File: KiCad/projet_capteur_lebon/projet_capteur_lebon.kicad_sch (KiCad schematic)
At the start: 19 parts, among them J1 Power, J2 Digital/PWM, J3 Analog, J4 Digital/PWM

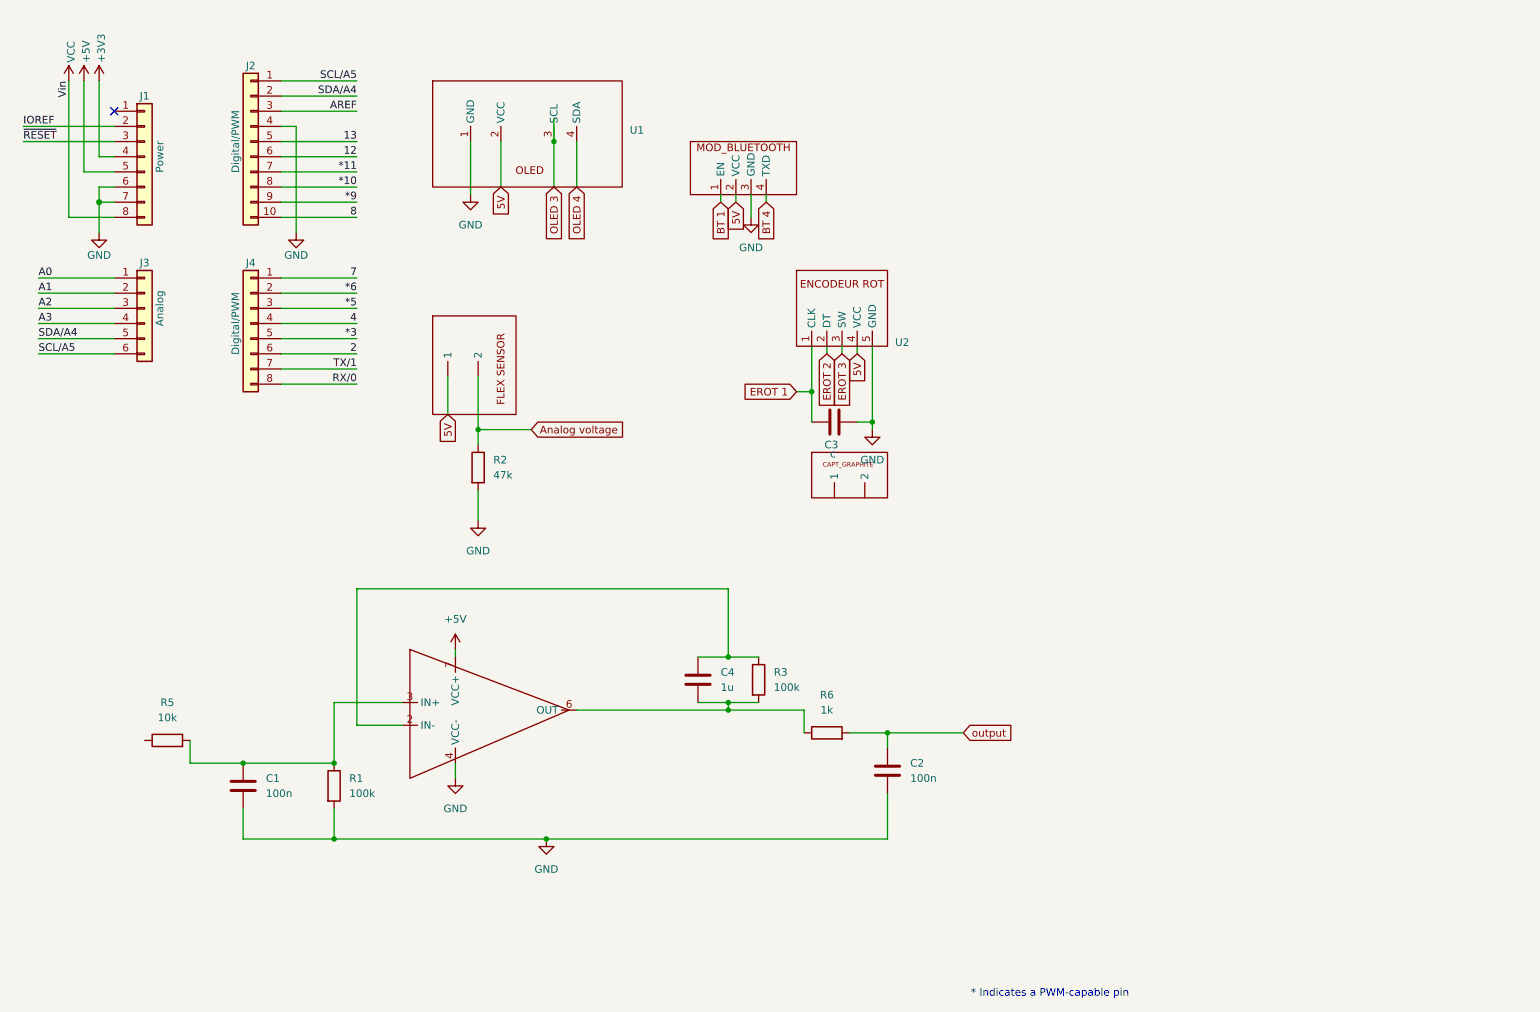
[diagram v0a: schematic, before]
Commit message: etiquettes + digital pot
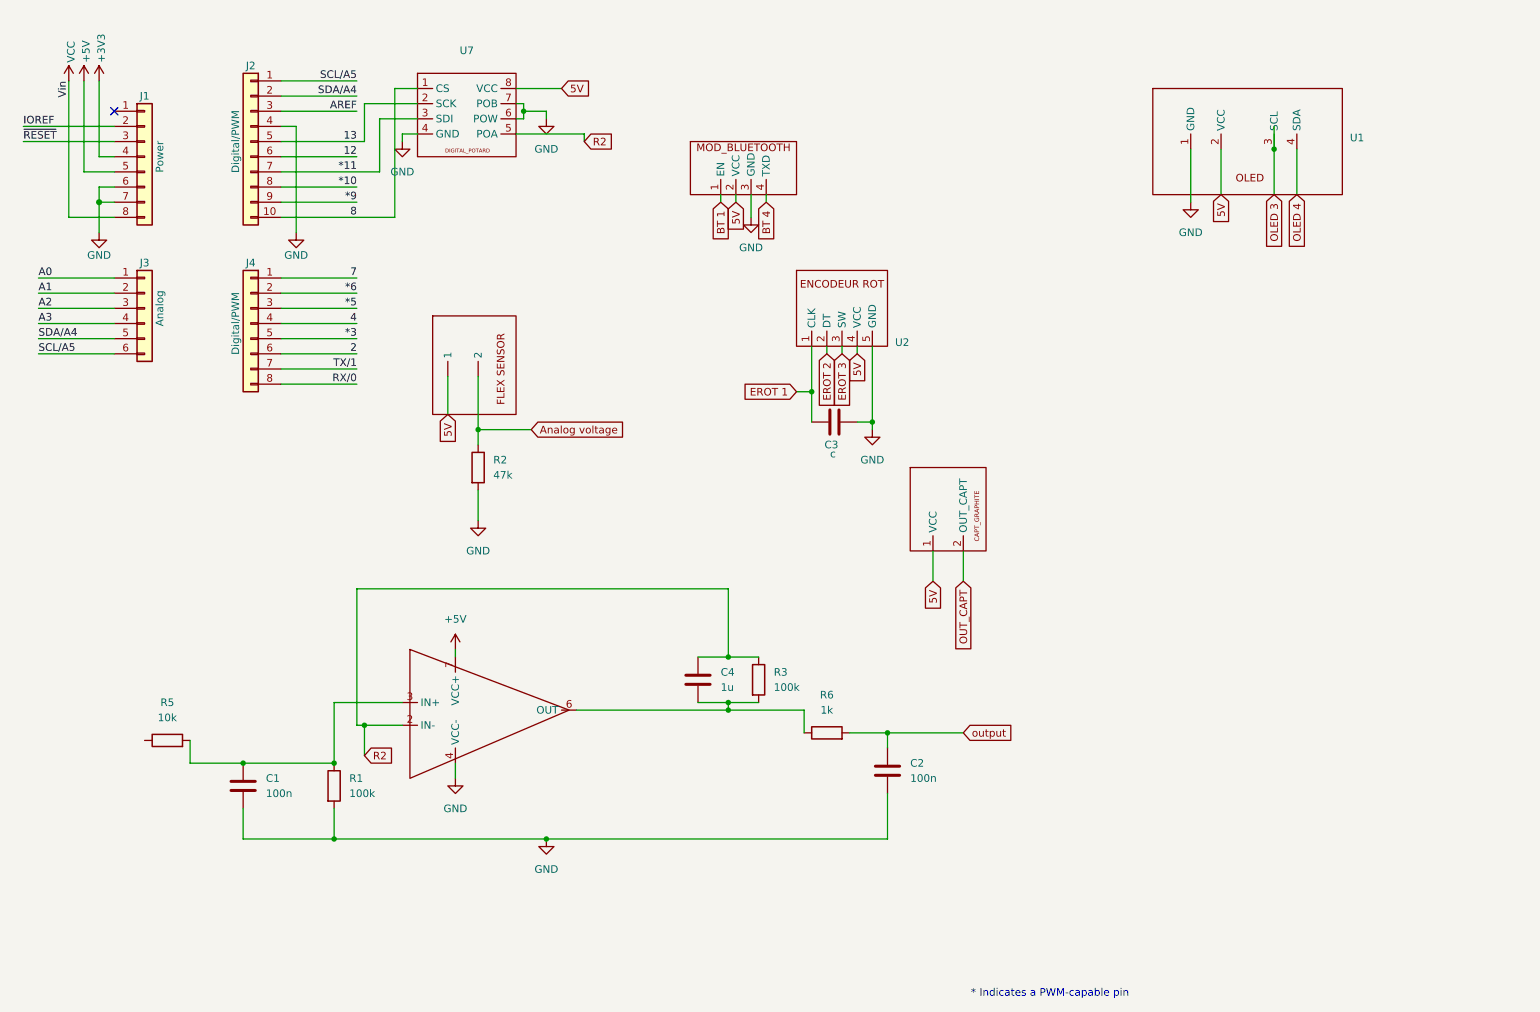
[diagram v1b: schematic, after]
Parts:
- removed U6: ~, librairie_empreintes:CAPTEUR_GRAPHITE, symbol librairie symboles:CAPTEUR_GRAPHITE
- added U7: ~, librairie_empreintes:DIP-8_296, symbol librairie symboles:DIGIT_POTARD
- added U8: ~, librairie_empreintes:CAPTEUR_GRAPHITE, symbol librairie symboles:CAPTEUR_GRAPHITE
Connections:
- net *11: now also U7.3 (SDI)
- net 13: now also U7.2 (SCK)
- net 5V: now also U7.8 (VCC), U8.1 (VCC)
- net 8: now also U7.1 (CS)
- net GND: now also U7.4 (GND), U7.6 (POW), U7.7 (POB)
- net R2: now reaches C4.1, R3.1, U4.2 (IN-)
- net R2: now also U7.5 (POA)
- new net OUT_CAPT: U8.2 (OUT_CAPT)
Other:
- moved on the sheet: U1

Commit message: fin schématique liaisons etc reste debug U5
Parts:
- removed U3: ~, librairie_empreintes:SIP-2, symbol librairie symboles:MOD_BLUETOOTH
- added U6: ~, librairie_empreintes:SIP-3, symbol librairie symboles:SERVOMOTOR
- added U9: ~, librairie_empreintes:BLUETOOTH, symbol librairie symboles:MOD_BLUETOOTH
- U5: footprint librairie_empreintes:BLUETOOTH -> librairie_empreintes:SIP-2
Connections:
- net AREF is gone; now on net 13: J2.3 (Pin_3)
- net Analog voltage is gone; now on net OUT_FLEX: R2.1, U5. (2)
- net EROT 1 is gone; now on net CLK: C3.1, U2.1 (CLK)
- net EROT 2 is gone; now on net DT: U2.2 (DT)
- net EROT 3 is gone; now on net SW: U2.3 (SW)
- net SCL/A5 is gone; now on net SCL: J2.1 (Pin_1), J3.6 (Pin_6)
- net SDA/A4 is gone; now on net SDA: J2.2 (Pin_2), J3.5 (Pin_5)
- net output is gone; now on net CAPT_AMPL: C2.1, R6.2
- net *10: now also U7.1 (CS)
- net *9: now also U6.1 (Data)
- net +5V: no longer J1.5 (Pin_5)
- net 5V: now also J1.5 (Pin_5), U6.2 (VCC), U9.2 (VCC)
- net GND: now also U6.3 (GND), U9.3 (GND)
- net OUT_CAPT: now also R5.1
- net *6 renamed SW
- net 2 renamed CLK
- net 4 renamed DT
- net 7 renamed RX
- net RX: now also U9.5 (RX)
- net 8 renamed TXD
- net TXD: now also U9.4 (TXD); no longer U7.1 (CS)
- net A0 renamed CAPT_AMPL
- net A1 renamed OUT_FLEX
- net OLED 3 renamed SCL
- net OLED 4 renamed SDA
- no-connect marks 1 -> 12
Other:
- moved on the sheet: C1, C2, C3, C4, J1, J2, J3, J4, R1, R2, R3, R5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

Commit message: modeles 3d et routage
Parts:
- renumbered R2 to R4
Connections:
- net +5V is gone; now on net 5V: U4.7 (VCC+)
- net 13: no longer J2.3 (Pin_3)
- net 5V: now also U5.1 (Vcc); no longer U5. (2)
- net OUT_FLEX: now also U5.2 (Out); no longer U5. (2)
- new net AREF: J2.3 (Pin_3)
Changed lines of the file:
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@@
 	)
 	(junction
-		(at 83.82 29.21)
-		(diameter 0)
-		(color 0 0 0 0)
-	)
-	(junction
 		(at 92.71 101.6)
 		(diameter 0)
@@
 	)
 	(junction
-		(at 71.12 41.91)
-		(diameter 0)
-		(color 0 0 0 0)
-	)
-	(junction
 		(at 153.67 90.17)
 		(diameter 0)
@@
 	)
 	(junction
-		(at 71.12 44.45)
-		(diameter 0)
-		(color 0 0 0 0)
-	)
-	(junction
 		(at 110.49 29.21)
 		(diameter 0)
@@
 	(wire
 		(pts
-			(xy 69.85 41.91) (xy 71.12 41.91)
-		)
-		(stroke
-			(width 0)
-			(type solid)
-		)
-	)
-	(wire
-		(pts
 			(xy 114.3 30.48) (xy 114.3 29.21)
 		)
@@
 	(wire
 		(pts
-			(xy 88.9 25.4) (xy 88.9 41.91)
+			(xy 87.63 25.4) (xy 87.63 41.91)
 		)
 		(stroke
@@
 	(wire
 		(pts
-			(xy 40.64 36.83) (xy 43.18 36.83)
+			(xy 85.09 34.29) (xy 85.09 27.94)
 		)
 		(stroke
@@
 	(wire
 		(pts
-			(xy 38.1 39.37) (xy 43.18 39.37)
+			(xy 40.64 36.83) (xy 43.18 36.83)
 		)
 		(stroke
@@
 	(wire
 		(pts
-			(xy 38.1 24.13) (xy 38.1 39.37)
+			(xy 38.1 39.37) (xy 43.18 39.37)
 		)
 		(stroke
@@
 	(wire
 		(pts
-			(xy 148.59 97.79) (xy 153.67 97.79)
+			(xy 38.1 24.13) (xy 38.1 39.37)
 		)
 		(stroke
 			(width 0)
-			(type default)
+			(type solid)
 		)
 	)
 	(wire
 		(pts
-			(xy 83.82 27.94) (xy 83.82 29.21)
+			(xy 148.59 97.79) (xy 153.67 97.79)
 		)
 		(stroke
@@
 	(wire
 		(pts
-			(xy 71.12 34.29) (xy 83.82 34.29)
+			(xy 71.12 34.29) (xy 85.09 34.29)
 		)
 		(stroke
@@
 	(wire
 		(pts
-			(xy 92.71 25.4) (xy 88.9 25.4)
+			(xy 92.71 25.4) (xy 87.63 25.4)
 		)
 		(stroke
@@
 	(wire
 		(pts
-			(xy 71.12 41.91) (xy 88.9 41.91)
+			(xy 71.12 44.45) (xy 92.71 44.45)
 		)
 		(stroke
 			(width 0)
-			(type solid)
+			(type default)
 		)
 	)
@@
 	(wire
 		(pts
-			(xy 92.71 27.94) (xy 83.82 27.94)
-		)
-		(stroke
-			(width 0)
-			(type default)
-		)
-	)
-	(wire
-		(pts
 			(xy 209.55 38.1) (xy 209.55 48.26)
 		)
@@
 	(wire
 		(pts
-			(xy 30.48 64.77) (xy 43.18 64.77)
-		)
-		(stroke
-			(width 0)
-			(type solid)
-		)
-	)
-	(wire
-		(pts
-			(xy 214.63 38.1) (xy 214.63 45.72)
+			(xy 71.12 41.91) (xy 87.63 41.91)
 		)
 		(stroke
@@
 	(wire
 		(pts
-			(xy 71.12 44.45) (xy 92.71 44.45)
+			(xy 30.48 64.77) (xy 43.18 64.77)
 		)
 		(stroke
 			(width 0)
-			(type default)
+			(type solid)
 		)
 	)
 	(wire
 		(pts
-			(xy 83.82 29.21) (xy 83.82 34.29)
+			(xy 214.63 38.1) (xy 214.63 45.72)
 		)
 		(stroke
@@
 	(wire
 		(pts
-			(xy 71.12 67.31) (xy 83.82 67.31)
+			(xy 85.09 27.94) (xy 92.71 27.94)
 		)
 		(stroke
@@
 	(wire
 		(pts
-			(xy 153.67 90.17) (xy 158.75 90.17)
+			(xy 71.12 67.31) (xy 83.82 67.31)
 		)
 		(stroke
 			(width 0)
-			(type default)
+			(type solid)
 		)
 	)
 	(wire
 		(pts
-			(xy 72.39 107.95) (xy 87.63 107.95)
+			(xy 153.67 90.17) (xy 158.75 90.17)
 		)
 		(stroke
@@
 	(wire
 		(pts
-			(xy 69.85 44.45) (xy 71.12 44.45)
+			(xy 72.39 107.95) (xy 87.63 107.95)
 		)
 		(stroke
@@
 	)
 	(label "*10"
-		(at 82.55 41.91 180)
+		(at 81.28 41.91 180)
 		(effects
 			(font
@@
 		)
 	)
+	(global_label "5V"
+		(shape input)
+		(at 107.95 88.9 90)
+		(fields_autoplaced yes)
+		(effects
+			(font
+				(size 1.27 1.27)
+			)
+			(justify left)
+		)
+		(property "Intersheetrefs" "${INTERSHEET_REFS}"
+			(at 107.95 83.5216 90)
+			(effects
+				(font
+					(size 1.27 1.27)
+				)
+				(justify left)
+				(hide yes)
+			)
+		)
+	)
 	(global_label "OUT_FLEX"
 		(shape input)
@@
 			)
 		)
-		(pin ""
+		(pin "2"
 		)
-		(pin ""
+		(pin "1"
 		)
 		(instances
@@
 		(dnp no)
 		(fields_autoplaced yes)
-		(property "Reference" "R2"
+		(property "Reference" "R4"
 			(at 223.52 81.2799 0)
 			(effects
@@
 			(project "projet_capteur_lebon"
 				(path "/e63e39d7-6ac0-4ffd-8aa3-1841a4541b55"
-					(reference "R2")
+					(reference "R4")
 					(unit 1)
 				)
@@
 					(unit 1)
 				)
-			)
-		)
-	)
-	(symbol
-		(lib_id "power:+5V")
-		(at 107.95 88.9 0)
-		(unit 1)
-		(exclude_from_sim no)
-		(in_bom yes)
-		(on_board yes)
-		(dnp no)
-		(fields_autoplaced yes)
-		(property "Reference" "#PWR07"
-			(at 107.95 92.71 0)
-			(effects
-				(font
-					(size 1.27 1.27)
-				)
-				(hide yes)
-			)
-		)
-		(property "Value" "+5V"
-			(at 107.95 83.82 0)
-			(effects
-				(font
-					(size 1.27 1.27)
-				)
-			)
-		)
-		(property "Footprint" ""
-			(at 107.95 88.9 0)
-			(effects
-				(font
-					(size 1.27 1.27)
-				)
-				(hide yes)
-			)
-		)
-		(property "Datasheet" ""
-			(at 107.95 88.9 0)
-			(effects
-				(font
-					(size 1.27 1.27)
-				)
-				(hide yes)
-			)
-		)
-		(property "Description" "Power symbol creates a global label with name \"+5V\""
-			(at 107.95 88.9 0)
-			(effects
-				(font
-					(size 1.27 1.27)
-				)
-				(hide yes)
-			)
-		)
-		(pin "1"
-		)
-		(instances
-			(project ""
-				(path "/e63e39d7-6ac0-4ffd-8aa3-1841a4541b55"
-					(reference "#PWR07")
-					(unit 1)
-				)

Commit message: finitions pcb et gerber
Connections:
- net GND: now also U7.5 (POA); no longer U7.7 (POB)
- net R2: now also U7.7 (POB); no longer U7.5 (POA)
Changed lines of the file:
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@@
 	)
 	(junction
-		(at 153.67 97.79)
+		(at 110.49 31.75)
 		(diameter 0)
 		(color 0 0 0 0)
 	)
 	(junction
-		(at 153.67 90.17)
+		(at 153.67 97.79)
 		(diameter 0)
 		(color 0 0 0 0)
 	)
 	(junction
-		(at 72.39 107.95)
+		(at 153.67 90.17)
 		(diameter 0)
 		(color 0 0 0 0)
 	)
 	(junction
-		(at 184.15 49.53)
+		(at 72.39 107.95)
 		(diameter 0)
 		(color 0 0 0 0)
 	)
 	(junction
-		(at 110.49 29.21)
+		(at 184.15 49.53)
 		(diameter 0)
 		(color 0 0 0 0)
@@
 	(wire
 		(pts
-			(xy 109.22 27.94) (xy 110.49 27.94)
+			(xy 109.22 27.94) (xy 119.38 27.94)
 		)
 		(stroke
@@
 	(wire
 		(pts
-			(xy 114.3 30.48) (xy 114.3 29.21)
-		)
-		(stroke
-			(width 0)
-			(type default)
-		)
-	)
-	(wire
-		(pts
 			(xy 71.12 24.13) (xy 83.82 24.13)
 		)
@@
 	(wire
 		(pts
+			(xy 114.3 31.75) (xy 114.3 35.56)
+		)
+		(stroke
+			(width 0)
+			(type default)
+		)
+	)
+	(wire
+		(pts
 			(xy 87.63 120.65) (xy 123.19 120.65)
 		)
@@
 	(wire
 		(pts
+			(xy 119.38 27.94) (xy 119.38 33.02)
+		)
+		(stroke
+			(width 0)
+			(type default)
+		)
+	)
+	(wire
+		(pts
+			(xy 110.49 33.02) (xy 109.22 33.02)
+		)
+		(stroke
+			(width 0)
+			(type default)
+		)
+	)
+	(wire
+		(pts
 			(xy 181.61 36.83) (xy 181.61 38.1)
 		)
@@
 	(wire
 		(pts
+			(xy 119.38 33.02) (xy 121.92 33.02)
+		)
+		(stroke
+			(width 0)
+			(type default)
+		)
+	)
+	(wire
+		(pts
 			(xy 220.98 67.31) (xy 220.98 76.2)
 		)
@@
 	(wire
 		(pts
-			(xy 109.22 33.02) (xy 120.65 33.02)
-		)
-		(stroke
-			(width 0)
-			(type default)
-		)
-	)
-	(wire
-		(pts
-			(xy 110.49 27.94) (xy 110.49 29.21)
+			(xy 110.49 31.75) (xy 114.3 31.75)
 		)
 		(stroke
@@
 	(wire
 		(pts
-			(xy 114.3 29.21) (xy 110.49 29.21)
-		)
-		(stroke
-			(width 0)
-			(type default)
-		)
-	)
-	(wire
-		(pts
 			(xy 43.18 41.91) (xy 40.64 41.91)
 		)
@@
 	(wire
 		(pts
-			(xy 110.49 29.21) (xy 110.49 30.48)
-		)
-		(stroke
-			(width 0)
-			(type default)
-		)
-	)
-	(wire
-		(pts
 			(xy 91.44 101.6) (xy 92.71 101.6)
 		)
@@
 	(wire
 		(pts
+			(xy 110.49 30.48) (xy 110.49 31.75)
+		)
+		(stroke
+			(width 0)
+			(type default)
+		)
+	)
+	(wire
+		(pts
 			(xy 72.39 107.95) (xy 87.63 107.95)
 		)
@@
 	(wire
 		(pts
-			(xy 120.65 33.02) (xy 120.65 34.29)
+			(xy 121.92 33.02) (xy 121.92 31.75)
+		)
+		(stroke
+			(width 0)
+			(type default)
+		)
+	)
+	(wire
+		(pts
+			(xy 110.49 31.75) (xy 110.49 33.02)
 		)
 		(stroke
@@
 	(global_label "R2"
 		(shape input)
-		(at 120.65 34.29 0)
+		(at 121.92 31.75 0)
 		(fields_autoplaced yes)
 		(effects
@@
 		)
 		(property "Intersheetrefs" "${INTERSHEET_REFS}"
-			(at 126.2098 34.29 0)
+			(at 127.4798 31.75 0)
 			(effects
 				(font
@@
 	(symbol
 		(lib_id "power:GND")
-		(at 114.3 30.48 0)
+		(at 114.3 35.56 0)
 		(unit 1)
 		(exclude_from_sim no)
@@
 		(fields_autoplaced yes)
 		(property "Reference" "#PWR014"
-			(at 114.3 36.83 0)
+			(at 114.3 41.91 0)
 			(effects
 				(font
@@
 		)
 		(property "Value" "GND"
-			(at 114.3 35.56 0)
+			(at 114.3 40.64 0)
 			(effects
 				(font
@@
 		)
 		(property "Footprint" ""
-			(at 114.3 30.48 0)
+			(at 114.3 35.56 0)
 			(effects
 				(font
@@
 		)
 		(property "Datasheet" ""
-			(at 114.3 30.48 0)
+			(at 114.3 35.56 0)
 			(effects
 				(font
@@
 		)
 		(property "Description" "Power symbol creates a global label with name \"GND\" , ground"
-			(at 114.3 30.48 0)
+			(at 114.3 35.56 0)
 			(effects
 				(font

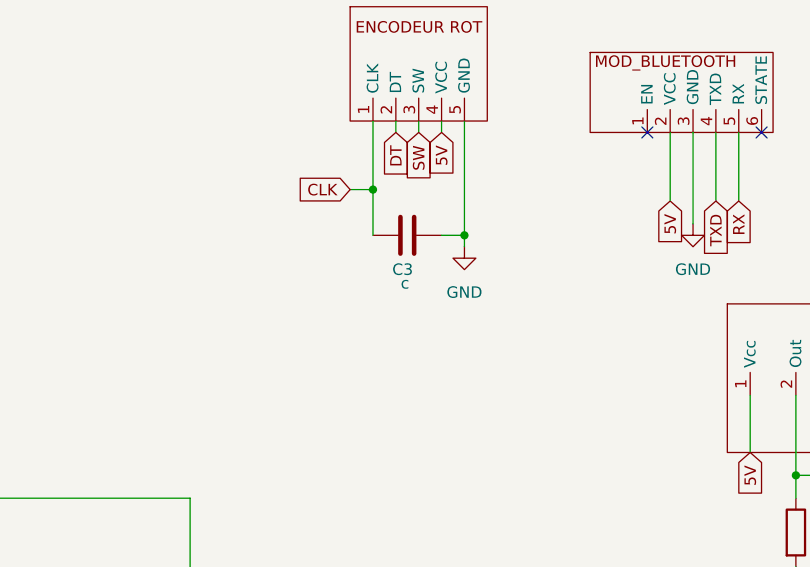
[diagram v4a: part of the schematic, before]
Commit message: capa c3 valeur
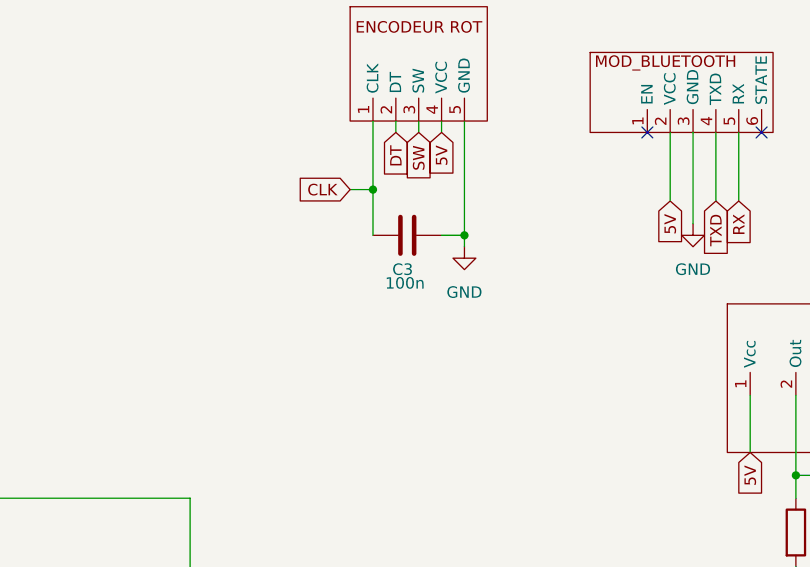
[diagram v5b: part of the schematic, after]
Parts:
- C3: value c -> 100n
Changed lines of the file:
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@@
 			)
 		)
-		(property "Value" "c"
+		(property "Value" "100n"
 			(at 177.546 54.864 90)
 			(effects
